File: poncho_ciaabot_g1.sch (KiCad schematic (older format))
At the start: 4 parts, among them J4 CONN_02X04, J5 CONN_01X03, J6 CONN_01X03, J7 CONN_01X03

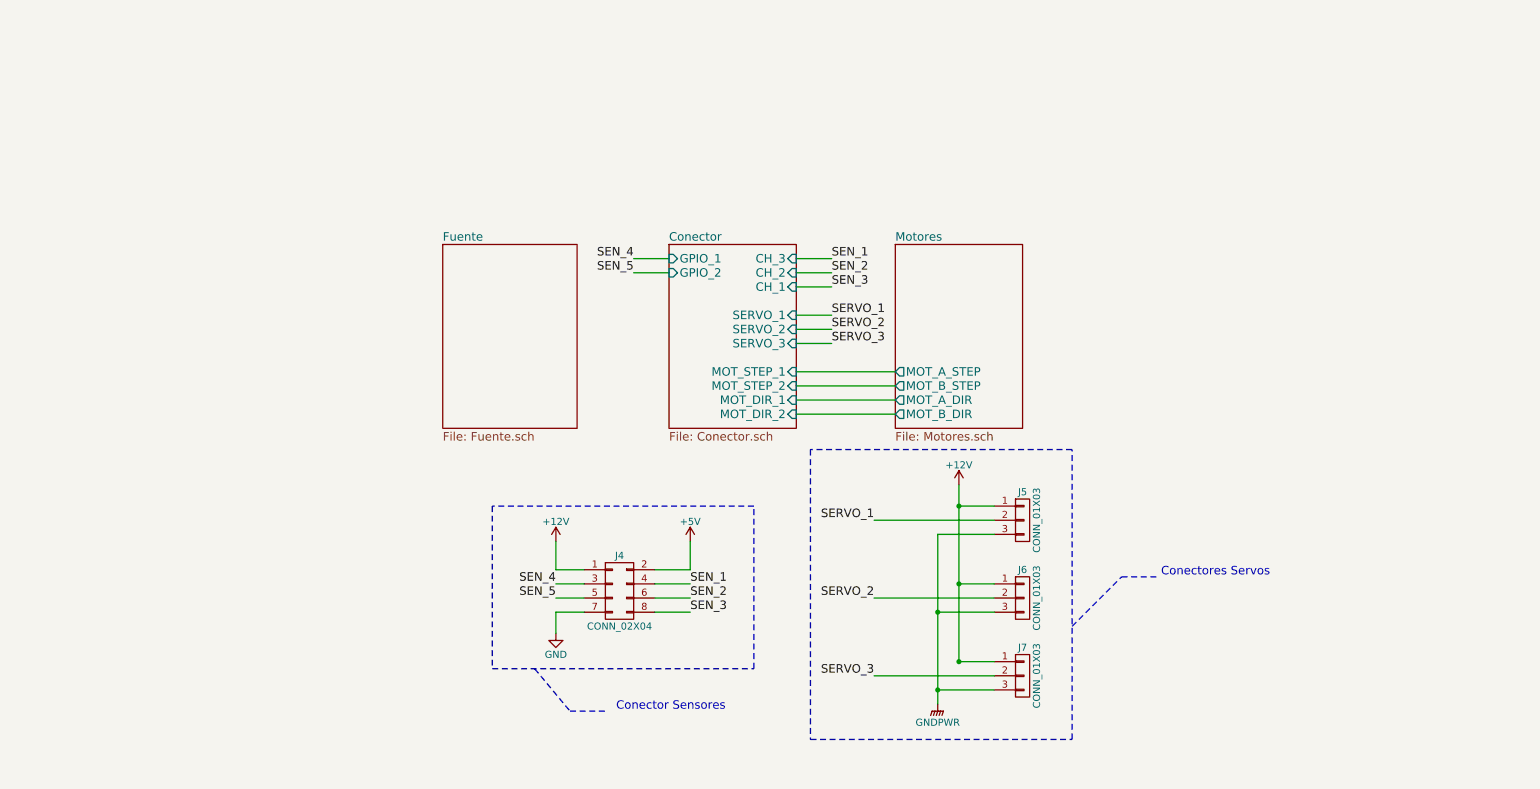
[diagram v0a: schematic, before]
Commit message: Reestructuracion de hojas de esquematico.
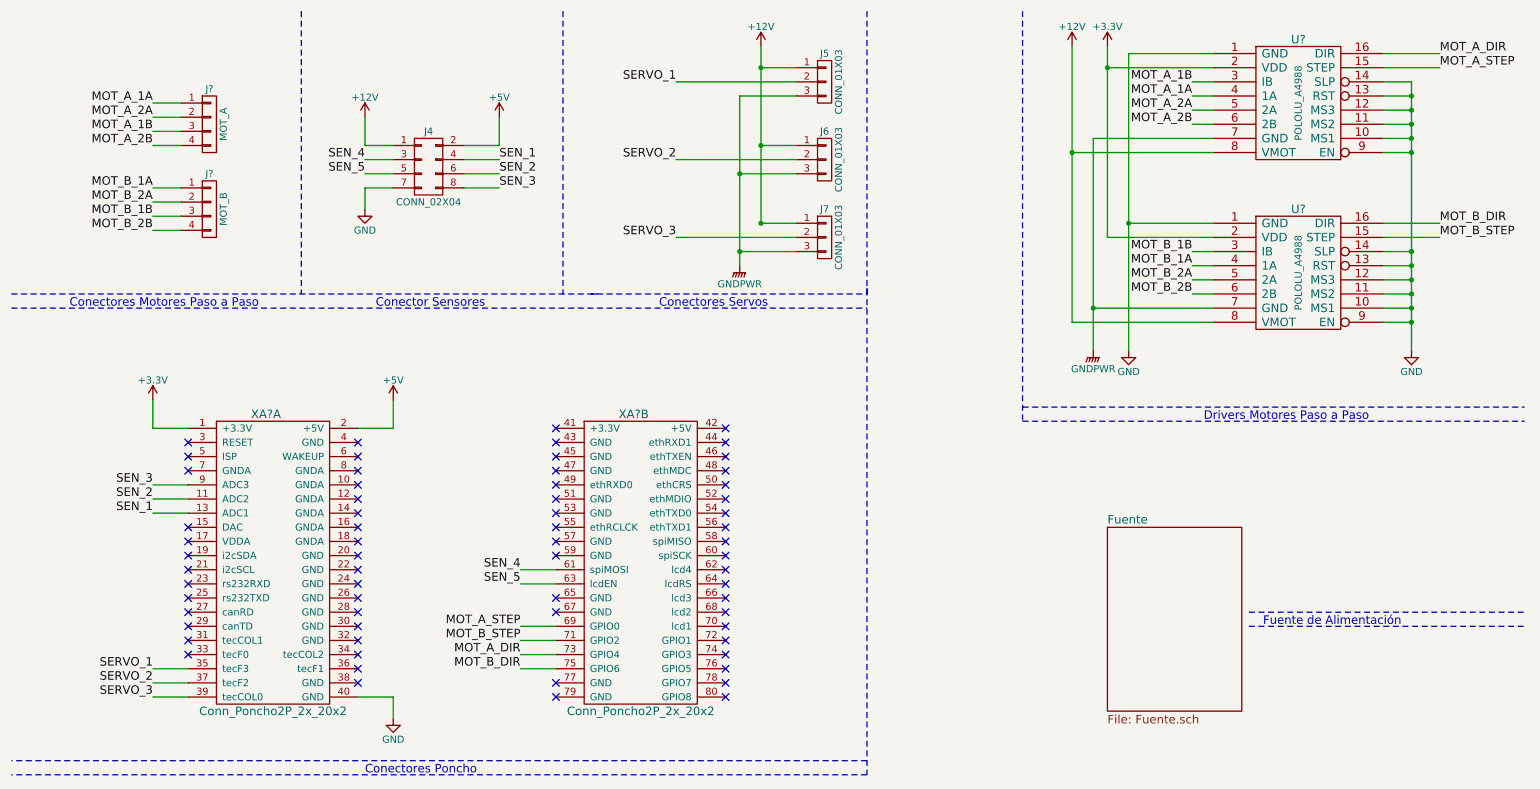
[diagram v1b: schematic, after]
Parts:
- added J?: MOT_A, symbol CONN_01X04
- added J?: MOT_B, symbol CONN_01X04
- added U? (x2): POLOLU_A4988, symbol POLOLU_A4988
- added XA? (x2): Conn_Poncho2P_2x_20x2, symbol Conn_Poncho2P_2x_20x2
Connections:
- net +12V: now also U?.8 (VMOT), U?.8 (VMOT)
- net +5V: now also XA?.2 (+5V)
- net GND: now also U?.1 (GND), U?.1 (GND), U?.10 (MS1), U?.10 (MS1), U?.11 (MS2), U?.11 (MS2), U?.12 (MS3), U?.12 (MS3), U?.13 (RST), U?.13 (RST), U?.14 (SLP), U?.14 (SLP), U?.9 (EN), U?.9 (EN), XA?.40 (GND)
- net GNDPWR: now also U?.7 (GND), U?.7 (GND)
- net SEN_1: now also XA?.13 (ADC1)
- net SEN_2: now also XA?.11 (ADC2)
- net SEN_3: now also XA?.9 (ADC3)
- net SEN_4: now also XA?.61 (spiMOSI)
- net SEN_5: now also XA?.63 (lcdEN)
- net SERVO_1: now also XA?.35 (tecF3)
- net SERVO_2: now also XA?.37 (tecF2)
- net SERVO_3: now also XA?.39 (tecCOL0)
- new net +3V3: U?.2 (VDD), U?.2 (VDD), XA?.1 (+3.3V)
- new net MOT_A_1A: J?.1 (P1), U?.4 (1A)
- new net MOT_A_1B: J?.3 (P3), U?.3 (IB)
- new net MOT_A_2A: J?.2 (P2), U?.5 (2A)
- new net MOT_A_2B: J?.4 (P4), U?.6 (2B)
- new net MOT_A_DIR: U?.16 (DIR), XA?.73 (GPIO4)
- new net MOT_A_STEP: U?.15 (STEP), XA?.69 (GPIO0)
- new net MOT_B_1A: J?.1 (P1), U?.4 (1A)
- new net MOT_B_1B: J?.3 (P3), U?.3 (IB)
- new net MOT_B_2A: J?.2 (P2), U?.5 (2A)
- new net MOT_B_2B: J?.4 (P4), U?.6 (2B)
- new net MOT_B_DIR: U?.16 (DIR), XA?.75 (GPIO6)
- new net MOT_B_STEP: U?.15 (STEP), XA?.71 (GPIO2)
- no-connect marks 0 -> 65
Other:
- note added: "Conectores Motores Paso a Paso"
- note added: "Conectores Poncho"
- note added: "Drivers Motores Paso a Paso"
- note added: "Fuente de Alimentación"
- moved on the sheet: J4, J5, J6, J7

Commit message: Se agregan codigos de DigiKey
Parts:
- J4: Digikey# (none) -> S7072-ND
- J5, J6, J7: Digikey# (none) -> S7001-ND
- J? (x2): Digikey# (none) -> S7002-ND
- XA? (x2): Digikey# (none) -> 952-1897-ND
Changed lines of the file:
@@
 F 2 "" H 3450 400 50  0001 C CNN
 F 3 "" H 3450 400 50  0001 C CNN
+F 4 "S7072-ND" H 3450 1600 60  0001 C CNN "Digikey#"
 	1    3450 1600
 	1    0    0    -1
@@
 F 2 "" H 6250 1000 50  0001 C CNN
 F 3 "" H 6250 1000 50  0001 C CNN
+F 4 "S7001-ND" H 6250 1000 60  0001 C CNN "Digikey#"
 	1    6250 1000
 	1    0    0    -1
@@
 F 2 "" H 6250 1550 50  0001 C CNN
 F 3 "" H 6250 1550 50  0001 C CNN
+F 4 "S7001-ND" H 6250 1550 60  0001 C CNN "Digikey#"
 	1    6250 1550
 	1    0    0    -1
@@
 F 2 "" H 6250 2100 50  0001 C CNN
 F 3 "" H 6250 2100 50  0001 C CNN
+F 4 "S7001-ND" H 6250 2100 60  0001 C CNN "Digikey#"
 	1    6250 2100
 	1    0    0    -1
@@
 F 2 "" H 1900 1300 50  0001 C CNN
 F 3 "" H 1900 1300 50  0001 C CNN
+F 4 "S7002-ND" H 1900 1300 60  0001 C CNN "Digikey#"
 	1    1900 1300
 	1    0    0    -1
@@
 F 2 "" H 1900 1900 50  0001 C CNN
 F 3 "" H 1900 1900 50  0001 C CNN
+F 4 "S7002-ND" H 1900 1900 60  0001 C CNN "Digikey#"
 	1    1900 1900
 	1    0    0    -1
@@
 F 2 "" H 2000 3750 60  0000 C CNN
 F 3 "" H 2000 3750 60  0000 C CNN
+F 4 "952-1897-ND" H 2000 3750 60  0001 C CNN "Digikey#"
 	1    2000 3750
 	1    0    0    -1
@@
 F 2 "" H 4600 3750 60  0000 C CNN
 F 3 "" H 4600 3750 60  0000 C CNN
+F 4 "952-1897-ND" H 4600 3750 60  0001 C CNN "Digikey#"
 	2    4600 3750
 	1    0    0    -1

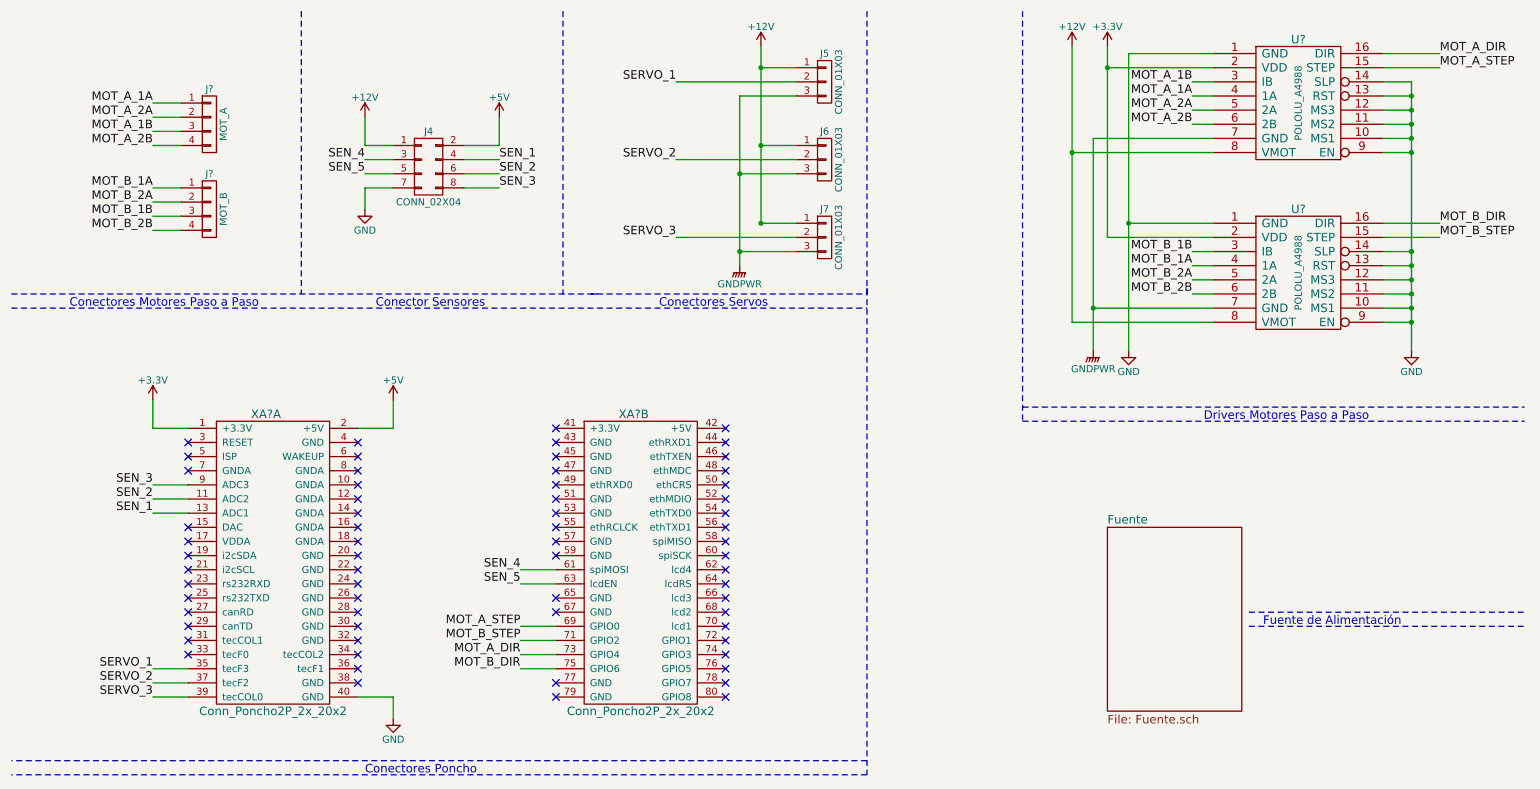
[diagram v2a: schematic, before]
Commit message: Se aplican las primeras correciones del profesor sobre esquematico
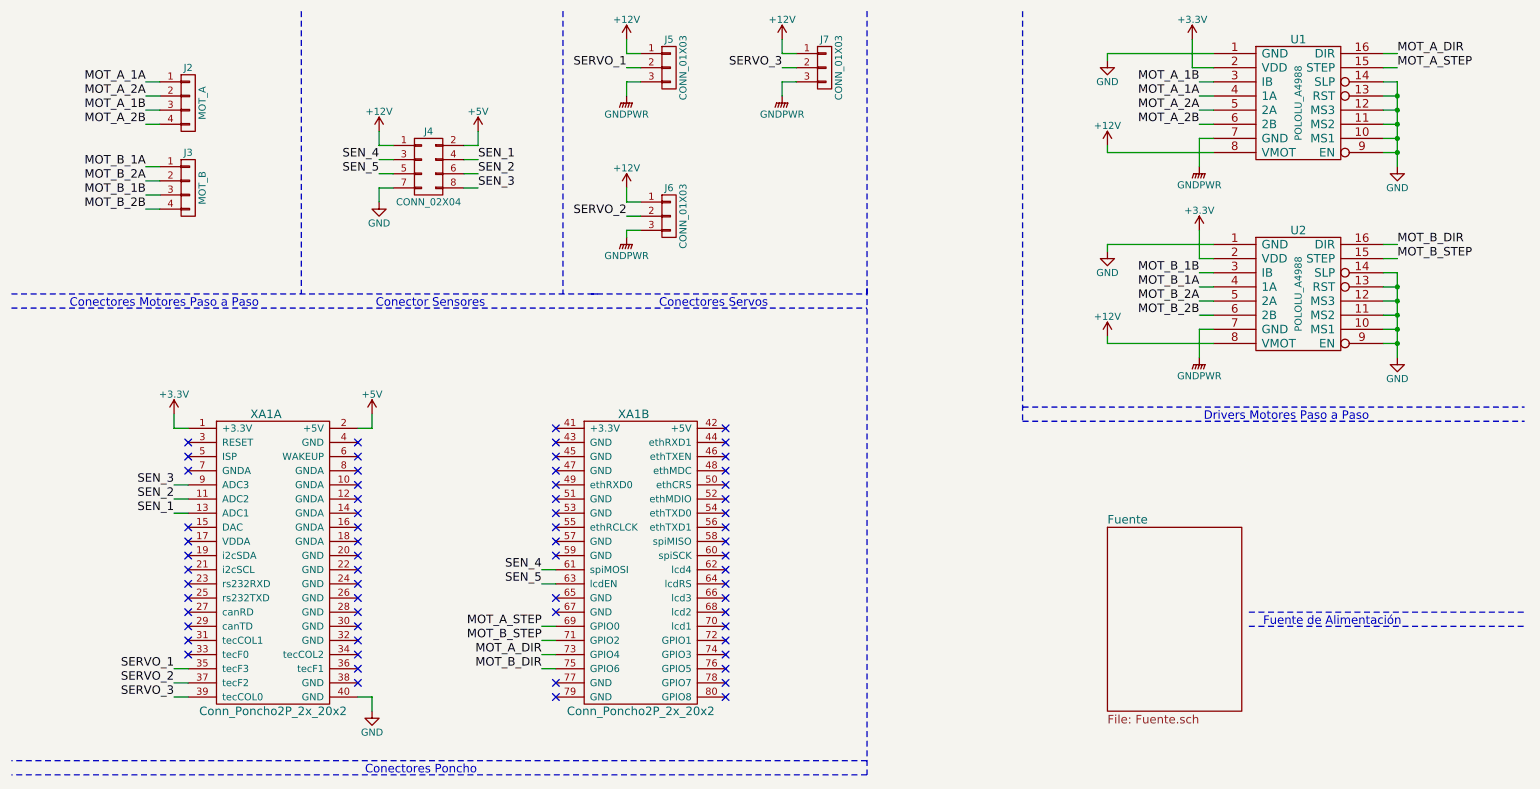
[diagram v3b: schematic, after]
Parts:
- J2, J3: renamed from J?; Manf (none) -> Sullins Connector Solutions; Manf# (none) -> PPTC041LFBN-RC
- J4: Manf (none) -> Sullins Connector Solutions; Manf# (none) -> PPTC042LFBN-RC
- J5, J6, J7: Manf (none) -> Sullins Connector Solutions; Manf# (none) -> PPTC031LFBN-RC
- U1, U2: renamed from U?; kicost:pricing (none) -> 1:$5.95; 5:$4.95; 25:$4.49; 100:$3.95
- XA1: renamed from XA?; Manf (none) -> Harwin Inc.; Manf# (none) -> M22-2522005
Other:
- moved on the sheet: J2, J3, J5, J6, J7, U2

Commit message: Primera version del PCB
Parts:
- J2, J3: footprint (none) -> Pin_Headers:Pin_Header_Straight_1x04_Pitch2.54mm
- J4: footprint (none) -> Pin_Headers:Pin_Header_Straight_2x04_Pitch2.54mm
- J5, J6, J7: footprint (none) -> Pin_Headers:Pin_Header_Straight_1x03_Pitch2.54mm
- U1, U2: footprint (none) -> ciaabot_g1:SWDIP8_.6W
- XA1: footprint (none) -> Poncho_Esqueleto:Conn_Poncho_Completo
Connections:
- net SEN_1: now also J4.8 (P8); no longer J4.4 (P4)
- net SEN_3: now also J4.4 (P4); no longer J4.8 (P8)
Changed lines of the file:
@@
 F 0 "J4" H 3450 1850 50  0000 C CNN
 F 1 "CONN_02X04" H 3450 1350 50  0000 C CNN
-F 2 "" H 3450 400 50  0001 C CNN
+F 2 "Pin_Headers:Pin_Header_Straight_2x04_Pitch2.54mm" H 3450 400 50  0001 C CNN
 F 3 "" H 3450 400 50  0001 C CNN
 F 4 "S7072-ND" H 3450 1600 60  0001 C CNN "Digikey#"
@@
 $EndComp
 Text Label 3800 1550 0    60   ~ 0
-SEN_1
+SEN_3
 Text Label 3800 1650 0    60   ~ 0
 SEN_2
 Text Label 3800 1750 0    60   ~ 0
-SEN_3
+SEN_1
 Text Label 3100 1550 2    60   ~ 0
 SEN_4
@@
 F 0 "J5" H 5150 1100 50  0000 C CNN
 F 1 "CONN_01X03" V 5250 900 50  0000 C CNN
-F 2 "" H 5150 900 50  0001 C CNN
+F 2 "Pin_Headers:Pin_Header_Straight_1x03_Pitch2.54mm" H 5150 900 50  0001 C CNN
 F 3 "" H 5150 900 50  0001 C CNN
 F 4 "S7001-ND" H 5150 900 60  0001 C CNN "Digikey#"
@@
 F 0 "J6" H 5150 2150 50  0000 C CNN
 F 1 "CONN_01X03" V 5250 1950 50  0000 C CNN
-F 2 "" H 5150 1950 50  0001 C CNN
+F 2 "Pin_Headers:Pin_Header_Straight_1x03_Pitch2.54mm" H 5150 1950 50  0001 C CNN
 F 3 "" H 5150 1950 50  0001 C CNN
 F 4 "S7001-ND" H 5150 1950 60  0001 C CNN "Digikey#"
@@
 F 0 "J7" H 6250 1100 50  0000 C CNN
 F 1 "CONN_01X03" V 6350 900 50  0000 C CNN
-F 2 "" H 6250 900 50  0001 C CNN
+F 2 "Pin_Headers:Pin_Header_Straight_1x03_Pitch2.54mm" H 6250 900 50  0001 C CNN
 F 3 "" H 6250 900 50  0001 C CNN
 F 4 "S7001-ND" H 6250 900 60  0001 C CNN "Digikey#"
@@
 F 0 "U1" H 9600 1600 60  0000 C CNN
 F 1 "POLOLU_A4988" V 9600 1150 50  0000 C CNN
-F 2 "" H 9600 1150 60  0001 C CNN
+F 2 "ciaabot_g1:SWDIP8_.6W" H 9600 1150 60  0001 C CNN
 F 3 "" H 9600 1150 60  0001 C CNN
 F 4 "1:$5.95; 5:$4.95; 25:$4.49; 100:$3.95" H 9600 1150 60  0001 C CNN "kicost:pricing"
@@
 F 0 "U2" H 9600 2950 60  0000 C CNN
 F 1 "POLOLU_A4988" V 9600 2500 50  0000 C CNN
-F 2 "" H 9600 2500 60  0001 C CNN
+F 2 "ciaabot_g1:SWDIP8_.6W" H 9600 2500 60  0001 C CNN
 F 3 "" H 9600 2500 60  0001 C CNN
 F 4 "1:$5.95; 5:$4.95; 25:$4.49; 100:$3.95" H 9600 2500 60  0001 C CNN "kicost:pricing"
@@
 F 0 "J2" H 1750 1400 50  0000 C CNN
 F 1 "MOT_A" V 1850 1150 50  0000 C CNN
-F 2 "" H 1750 1150 50  0001 C CNN
+F 2 "Pin_Headers:Pin_Header_Straight_1x04_Pitch2.54mm" H 1750 1150 50  0001 C CNN
 F 3 "" H 1750 1150 50  0001 C CNN
 F 4 "S7002-ND" H 1750 1150 60  0001 C CNN "Digikey#"
@@
 F 0 "J3" H 1750 2000 50  0000 C CNN
 F 1 "MOT_B" V 1850 1750 50  0000 C CNN
-F 2 "" H 1750 1750 50  0001 C CNN
+F 2 "Pin_Headers:Pin_Header_Straight_1x04_Pitch2.54mm" H 1750 1750 50  0001 C CNN
 F 3 "" H 1750 1750 50  0001 C CNN
 F 4 "S7002-ND" H 1750 1750 60  0001 C CNN "Digikey#"
@@
 F 0 "XA1" H 2300 4150 60  0000 C CNN
 F 1 "Conn_Poncho2P_2x_20x2" H 2350 2050 60  0000 C CNN
-F 2 "" H 2000 3750 60  0000 C CNN
+F 2 "Poncho_Esqueleto:Conn_Poncho_Completo" H 2000 3750 60  0001 C CNN
 F 3 "" H 2000 3750 60  0000 C CNN
 F 4 "952-1897-ND" H 2000 3750 60  0001 C CNN "Digikey#"
@@
 F 0 "XA1" H 4900 4150 60  0000 C CNN
 F 1 "Conn_Poncho2P_2x_20x2" H 4950 2050 60  0000 C CNN
-F 2 "" H 4600 3750 60  0000 C CNN
+F 2 "Poncho_Esqueleto:Conn_Poncho_Completo" H 4600 3750 60  0001 C CNN
 F 3 "" H 4600 3750 60  0000 C CNN
 F 4 "952-1897-ND" H 4600 3750 60  0001 C CNN "Digikey#"
